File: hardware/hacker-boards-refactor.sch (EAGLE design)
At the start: 8 parts, among them IC1 TS520550, X2 MINI-USB-UX60-MB-5S8

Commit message: Added USB parts, reset logic, headers, LEDs. Cleaned up.
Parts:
- removed IC1: TS520550, v-reg:TS520550
- removed X2: MINI-USB-UX60-MB-5S8, con-hirose:MINI-USB-UX60-MB-5S8
- added C1, C2, C5: 10uF, hacker-board:C0805
- added C3, C4: 1uF, hacker-board:C0805
- added D1, D2: (no value), hacker-board:LED0603
- added J1: MICRO_USB_B_JST_MC5BR3-M404-4S, hacker-board:MICRO_USB_B_JST_MC5BR3-M404-4S
- added R10, R4, R5, R6, R8, R9: 10k, resistor:R-US_R0805
- added R7: 1k, resistor:R-US_R0805
- added S1, S2: TAC_SWITCHSMD, hacker-board:TAC_SWITCHSMD
- added SV1, SV2: (no value), con-lsta:FE07-1
- added U$1: USB-FUSE, hacker-board:USB-FUSE
- added U$2: AP2112, hacker-board:AP2112
- added U$3: CP2104, hacker-board:CP2104
- added U$4: MBT3904DW1T1G, hacker-board:MBT3904DW1T1G
- LED1, LED2: value (none) -> WS2812B5050; device led:LEDCHIP-LED0603 -> hacker-board:WS2812B5050
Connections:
- removed net VBUS_UNREG: X2.1
- new net DTR: R10.2, U$3.DTR, U$4G$1.EMIT
- new net N$11: R10.1, U$4G$2.BASE
- new net N$5: LED1.DO, LED2.DI
- new net N$7: R8.2, U$2.EN
- new net N$8: R9.1, U$4G$1.BASE
- new net RTS: R9.2, U$3.RTS, U$4G$2.EMIT
- new net USB_RX: R7.1, U$3.TXD
- net +3V3: now also C2.1, C3.1, C5.1, LED1.VDD, LED2.VDD, R4.2, R5.2, SV1.7, U$2.VOUT, U$3.REGIN, U$3.VDD, U$3.VIO; no longer IC1.VOUT
- net +5V: now also C1.1, C4.1, R8.1, U$1.OUT, U$2.VIN; no longer IC1.CE, IC1.VIN
- net ANALOG_IN: now also SV1.4
- net CH_PD: now also R5.1
- net GND: now also C1.2, C2.2, C3.2, C4.2, C5.2, D1.C, J1.GND, LED1.GND, LED2.GND, R6.1, S1.1, S1.2, S2.1, S2.2, SV1.6, U$2.GND, U$3.GND; no longer IC1.CB, IC1.GND, LED1.C, X2.5
- net GPIO0: now also D2.C, S2.3, S2.4, SV1.1, U$4G$1.COL; no longer LED2.C
- net GPIO12: now also SV2.5
- net GPIO13: now also SV2.6
- net GPIO14: now also SV2.4
- net GPIO15: now also R6.2
- net GPIO16: now also SV2.1, SV2.7
- net GPIO2: now also LED1.DI, R4.1
- net GPIO4/SDA: now also SV2.2
- net GPIO5/SCL: now also SV2.3
- net N$1: now also D1.A; no longer LED1.A
- net N$2: now also J1.+5V, U$1.IN; no longer R2.1
- net N$3: now also D2.A; no longer LED2.A
- net RST: now also R2.1, S1.3, S1.4, SV1.5, U$4G$2.COL
- net RX: now also R7.2, SV1.3
- net TX: now also SV1.2, U$3.RXD
- net USB+: now also J1.D+, U$3.D+, U$3.VBUS; no longer X2.3
- net USB-: now also J1.D-, U$3.D-; no longer X2.2
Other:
- note added: "ESD Protection Here"
- note added: "ESP8266 Breakout Module"
- note added: "Headers"
- note added: "LEDs"
- note added: "Potentiometer"
- note added: "Power Distrubution"
- note added: "Reset Logic"
- note added: "USB Electronics"
- note removed: "CAP"
- note removed: "CONFIG"
- note removed: "ESD PROTECTION"
- note removed: "POWER LED"
- note removed: "REPLACE"
- note removed: "RESET"
- moved on the sheet: R1, R2, R3

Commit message: Current limiting resistor on data pin of WS2812, decoupling caps on power lines
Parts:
- added C6, C7: 1uF, hacker-board:C0805
- added R11: 1k, resistor:R-US_R0805
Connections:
- new net N$6: LED1.DI, R11.1
- net +3V3: now also C6.1, C7.1
- net GND: now also C6.2, C7.2
- net GPIO2: now also R11.2; no longer LED1.DI
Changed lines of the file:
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@@
 <part name="FRAME1" library="frames" deviceset="DINA3_L" device=""/>
 <part name="SV2" library="con-lsta" deviceset="FE07-1" device=""/>
+<part name="R11" library="resistor" deviceset="R-US_" device="R0805" value="1k"/>
+<part name="C6" library="hacker-board" deviceset="C" device="0805" value="1uF"/>
+<part name="C7" library="hacker-board" deviceset="C" device="0805" value="1uF"/>
 </parts>
 <sheets>
@@
 <instance part="LED1" gate="G$1" x="220.98" y="-20.32"/>
 <instance part="LED2" gate="G$1" x="251.46" y="-20.32"/>
-<instance part="GND7" gate="1" x="220.98" y="-33.02"/>
-<instance part="GND8" gate="1" x="251.46" y="-33.02"/>
-<instance part="+3V6" gate="G$1" x="226.06" y="-2.54"/>
-<instance part="+3V7" gate="G$1" x="256.54" y="-2.54"/>
+<instance part="GND7" gate="1" x="220.98" y="-38.1"/>
+<instance part="GND8" gate="1" x="251.46" y="-38.1"/>
+<instance part="+3V6" gate="G$1" x="226.06" y="2.54"/>
+<instance part="+3V7" gate="G$1" x="256.54" y="2.54"/>
 <instance part="R4" gate="G$1" x="124.46" y="66.04" rot="R90"/>
 <instance part="R5" gate="G$1" x="139.7" y="66.04" rot="R90"/>
@@
 <instance part="FRAME1" gate="G$2" x="193.04" y="-91.44"/>
 <instance part="SV2" gate="G$1" x="142.24" y="-66.04" rot="R180"/>
+<instance part="R11" gate="G$1" x="200.66" y="-22.86" rot="R180"/>
+<instance part="C6" gate="G$1" x="236.22" y="-7.62"/>
+<instance part="C7" gate="G$1" x="269.24" y="-7.62"/>
 </instances>
 <busses>
@@
 <pinref part="LED1" gate="G$1" pin="VDD"/>
 <pinref part="+3V6" gate="G$1" pin="+3V3"/>
+<wire x1="226.06" y1="0" x2="226.06" y2="-2.54" width="0.1524" layer="91"/>
+<pinref part="C6" gate="G$1" pin="1"/>
+<wire x1="226.06" y1="-2.54" x2="226.06" y2="-5.08" width="0.1524" layer="91"/>
+<wire x1="236.22" y1="-5.08" x2="236.22" y2="-2.54" width="0.1524" layer="91"/>
+<wire x1="236.22" y1="-2.54" x2="226.06" y2="-2.54" width="0.1524" layer="91"/>
+<junction x="226.06" y="-2.54"/>
 </segment>
 <segment>
 <pinref part="LED2" gate="G$1" pin="VDD"/>
 <pinref part="+3V7" gate="G$1" pin="+3V3"/>
+<wire x1="256.54" y1="0" x2="256.54" y2="-2.54" width="0.1524" layer="91"/>
+<pinref part="C7" gate="G$1" pin="1"/>
+<wire x1="256.54" y1="-2.54" x2="256.54" y2="-5.08" width="0.1524" layer="91"/>
+<wire x1="269.24" y1="-5.08" x2="269.24" y2="-2.54" width="0.1524" layer="91"/>
+<wire x1="269.24" y1="-2.54" x2="256.54" y2="-2.54" width="0.1524" layer="91"/>
+<junction x="256.54" y="-2.54"/>
 </segment>
 <segment>
@@
 <pinref part="LED1" gate="G$1" pin="GND"/>
 <pinref part="GND7" gate="1" pin="GND"/>
+<wire x1="220.98" y1="-35.56" x2="220.98" y2="-33.02" width="0.1524" layer="91"/>
+<pinref part="C6" gate="G$1" pin="2"/>
+<wire x1="236.22" y1="-12.7" x2="236.22" y2="-30.48" width="0.1524" layer="91"/>
+<wire x1="236.22" y1="-30.48" x2="220.98" y2="-30.48" width="0.1524" layer="91"/>
+<wire x1="220.98" y1="-30.48" x2="220.98" y2="-33.02" width="0.1524" layer="91"/>
 </segment>
 <segment>
 <pinref part="LED2" gate="G$1" pin="GND"/>
 <pinref part="GND8" gate="1" pin="GND"/>
+<wire x1="251.46" y1="-35.56" x2="251.46" y2="-30.48" width="0.1524" layer="91"/>
+<pinref part="C7" gate="G$1" pin="2"/>
+<wire x1="269.24" y1="-12.7" x2="269.24" y2="-30.48" width="0.1524" layer="91"/>
+<wire x1="269.24" y1="-30.48" x2="251.46" y2="-30.48" width="0.1524" layer="91"/>
+<junction x="251.46" y="-30.48"/>
 </segment>
 <segment>
@@
 </segment>
 <segment>
-<pinref part="LED1" gate="G$1" pin="DI"/>
-<wire x1="208.28" y1="-22.86" x2="200.66" y2="-22.86" width="0.1524" layer="91"/>
-<label x="200.66" y="-22.86" size="1.778" layer="95"/>
-</segment>
-<segment>
 <pinref part="R4" gate="G$1" pin="1"/>
 <wire x1="124.46" y1="60.96" x2="124.46" y2="45.72" width="0.1524" layer="91"/>
 <label x="124.46" y="45.72" size="1.778" layer="95" rot="R90"/>
+</segment>
+<segment>
+<pinref part="R11" gate="G$1" pin="2"/>
+<wire x1="195.58" y1="-22.86" x2="187.96" y2="-22.86" width="0.1524" layer="91"/>
+<label x="187.96" y="-22.86" size="1.778" layer="95"/>
 </segment>
 </net>
@@
 </segment>
 </net>
+<net name="N$6" class="0">
+<segment>
+<pinref part="R11" gate="G$1" pin="1"/>
+<pinref part="LED1" gate="G$1" pin="DI"/>
+<wire x1="205.74" y1="-22.86" x2="208.28" y2="-22.86" width="0.1524" layer="91"/>
+</segment>
+</net>

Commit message: Added potentiometer and ESD protection for USB
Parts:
- added R12, R13: VARISTORCN0603, varistor:VARISTORCN0603
- added R14: 750, resistor:R-US_R0805
- added R15: 330, resistor:R-US_R0805
- added SJ1: (no value), jumper:SJ
- added TM1: (no value), adafruit:TRIMPOTTC33X
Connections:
- new net N$12: SJ1.1, TM1.S
- new net N$4: R14.1, R15.2, TM1.E
- new net N$9: R13.1
- net +3V3: now also R14.2
- net ANALOG_IN: now also SJ1.2
- net GND: now also R12.2, R13.2, R15.1, TM1.A
- net USB+: now also R12.1
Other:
- note added: "Addressable WS2812b LEDs"
- note added: "Bourns CG0603MLC-05E"
- note added: "Control with IO pin 2"
- note added: "Maunal reset/mode"
- note added: "Mode LED"
- note added: "Power LED"
- note added: "Pull-up/pull-down resistors"
- note added: "Reset/bootloader mode from USB/UART chip"
- note added: "Static Discharge Protection"
- note added: "USB 5V to 3.3V (500mA limit)"
- note added: "USB Micro Connector"
- note added: "USB to Serial/UART"
- note removed: "ESD Protection Here"
- moved on the sheet: C1, C2, C3, R10, R2, R8, R9, S1, S2

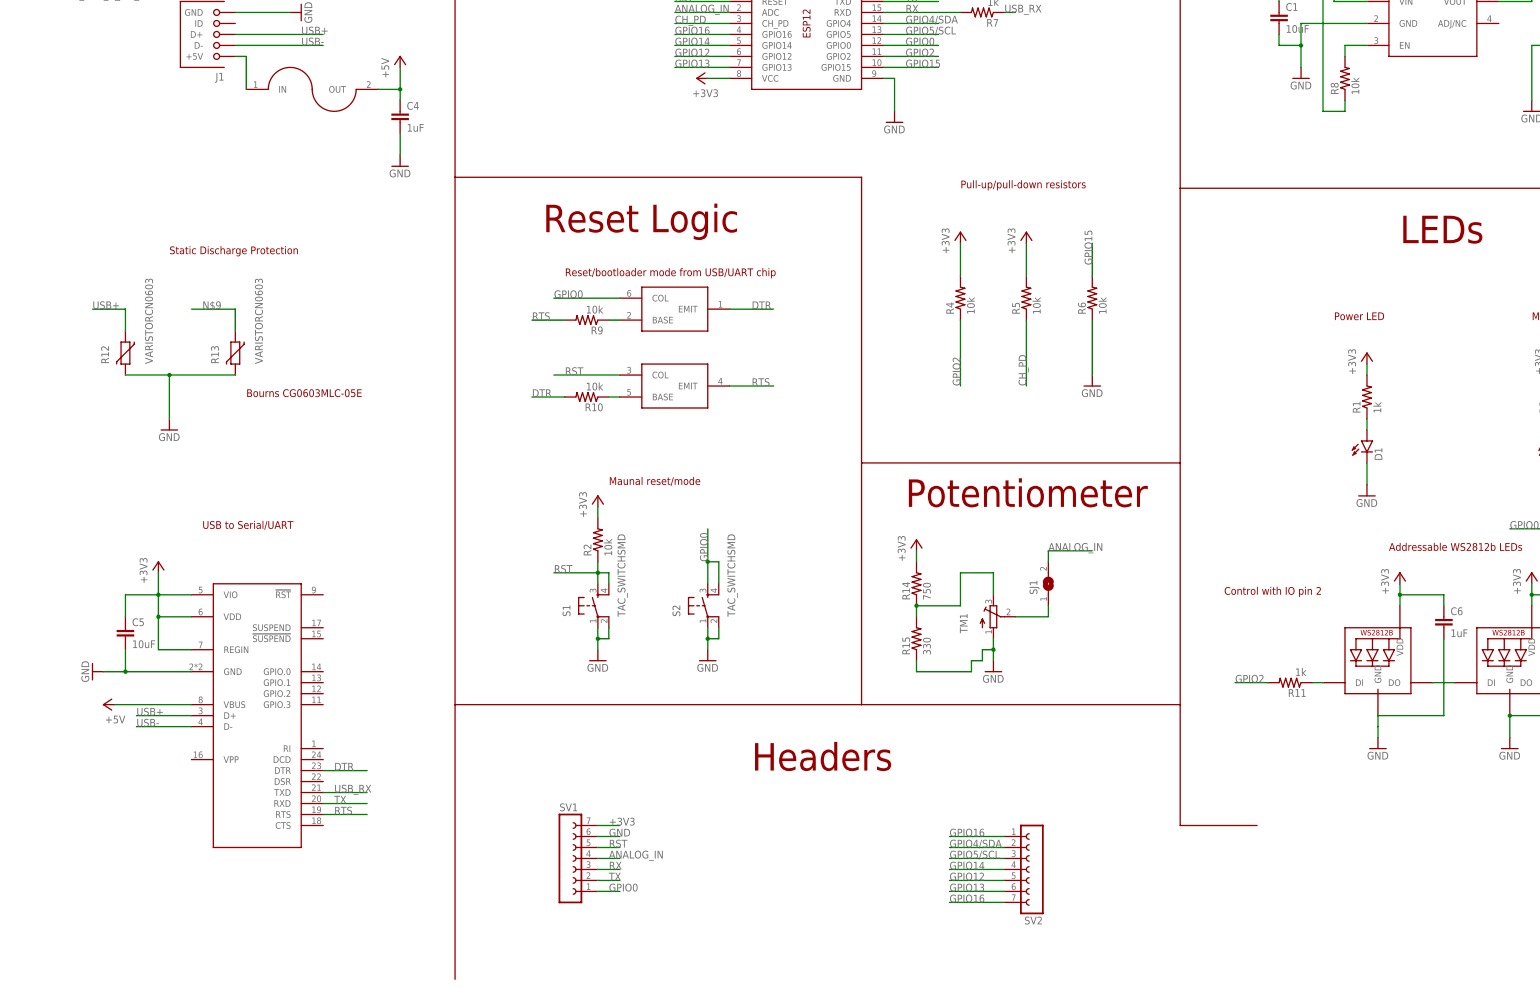
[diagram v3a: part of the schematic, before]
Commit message: Initial board commit (with autorouted traces), schematic cleanup
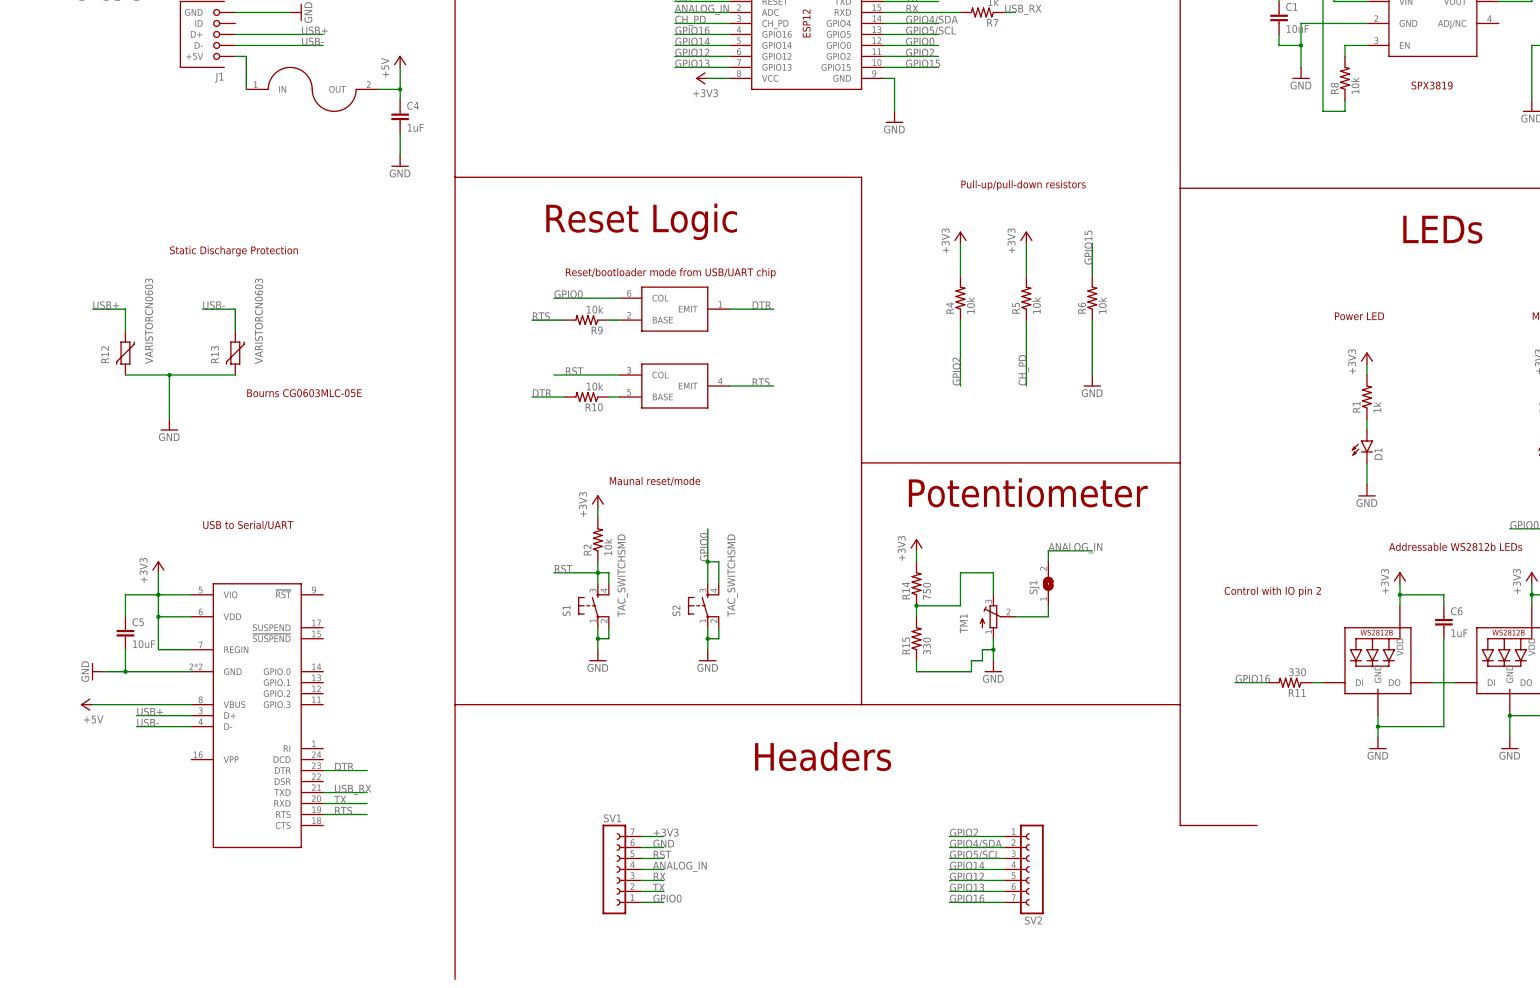
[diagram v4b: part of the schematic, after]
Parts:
- R11: value 1k -> 330
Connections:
- removed net N$9: R13.1
- net +5V: now also U$3.VBUS
- net GPIO16: now also R11.2; no longer SV2.1
- net GPIO2: now also SV2.1; no longer R11.2
- net USB+: no longer U$3.VBUS
- net USB-: now also R13.1
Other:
- note added: "SPX3819"
- moved on the sheet: SV1
